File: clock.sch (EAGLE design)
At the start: 15 parts, among them IC1 MEGA16-P

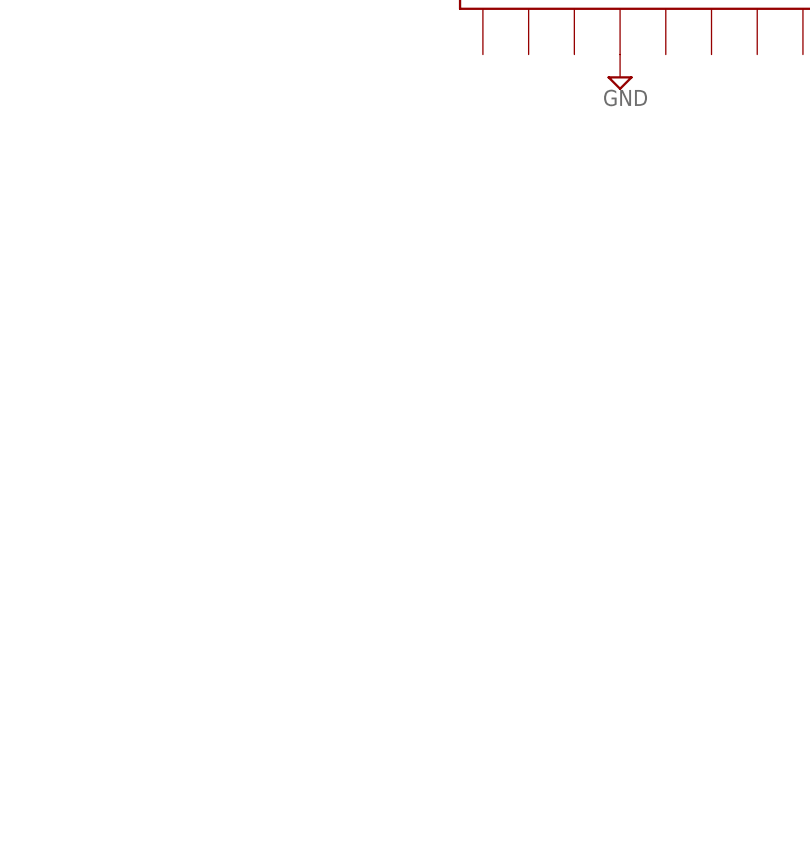
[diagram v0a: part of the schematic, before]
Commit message: 1.1
added smd leds and bugfixed a route.
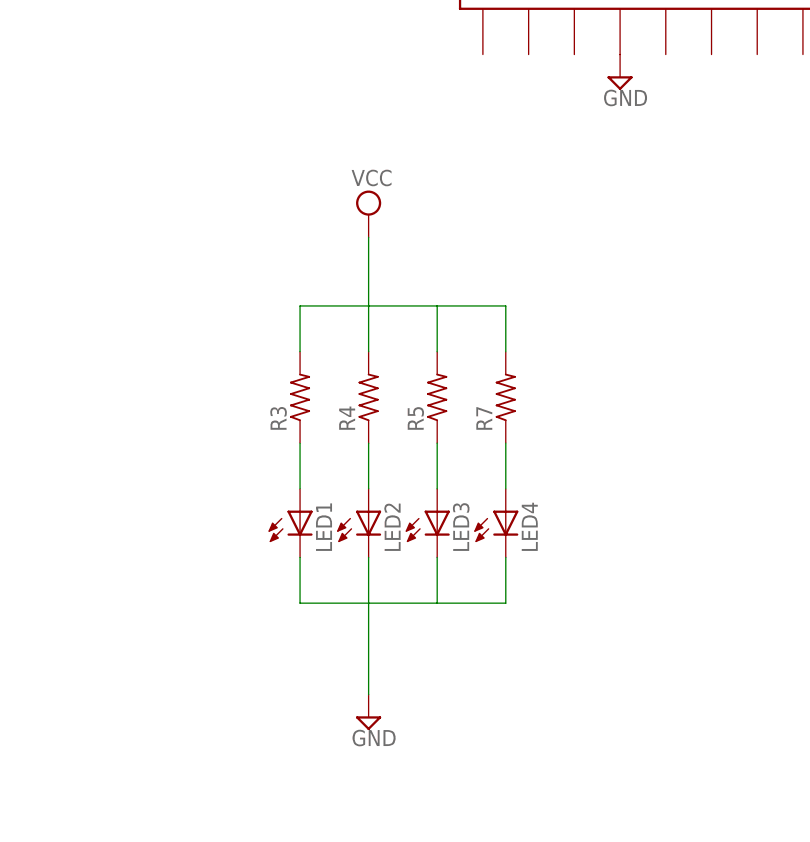
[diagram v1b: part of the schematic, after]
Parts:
- added LED1, LED2, LED3, LED4: (no value), eagle-ltspice:LED_ESML0603
- added R3, R4, R5, R7: (no value), resistor:R-US_R0603
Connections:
- new net N$15: LED1.A, R3.1
- new net N$18: LED2.A, R4.1
- new net N$27: LED3.A, R5.1
- new net N$28: LED4.A, R7.1
- net GND: now also LED1.C, LED2.C, LED3.C, LED4.C
- net VCC: now also R3.2, R4.2, R5.2, R7.2
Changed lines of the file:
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@@
 <layer number="97" name="Info" color="7" fill="1" visible="yes" active="yes"/>
 <layer number="98" name="Guide" color="6" fill="1" visible="yes" active="yes"/>
+<layer number="99" name="SpiceOrder" color="5" fill="1" visible="yes" active="yes"/>
 </layers>
 <schematic xreflabel="%F%N/%S.%C%R" xrefpart="/%S.%C%R">
@@
 <part name="SUPPLY13" library="supply2" deviceset="GND" device=""/>
 <part name="SUPPLY14" library="supply2" deviceset="VCC" device=""/>
+<part name="LED1" library="eagle-ltspice" deviceset="LED_E" device="SML0603"/>
+<part name="LED2" library="eagle-ltspice" deviceset="LED_E" device="SML0603"/>
+<part name="LED3" library="eagle-ltspice" deviceset="LED_E" device="SML0603"/>
+<part name="LED4" library="eagle-ltspice" deviceset="LED_E" device="SML0603"/>
+<part name="R3" library="resistor" deviceset="R-US_" device="R0603"/>
+<part name="R4" library="resistor" deviceset="R-US_" device="R0603"/>
+<part name="R5" library="resistor" deviceset="R-US_" device="R0603"/>
+<part name="R7" library="resistor" deviceset="R-US_" device="R0603"/>
+<part name="SUPPLY15" library="supply2" deviceset="VCC" device=""/>
+<part name="SUPPLY16" library="supply2" deviceset="GND" device=""/>
 </parts>
 <sheets>
@@
 <instance part="SUPPLY13" gate="GND" x="5.08" y="-17.78"/>
 <instance part="SUPPLY14" gate="G$1" x="-12.7" y="68.58" rot="R90"/>
+<instance part="LED1" gate="G$1" x="172.72" y="12.7"/>
+<instance part="LED2" gate="G$1" x="180.34" y="12.7"/>
+<instance part="LED3" gate="G$1" x="187.96" y="12.7"/>
+<instance part="LED4" gate="G$1" x="195.58" y="12.7"/>
+<instance part="R3" gate="G$1" x="172.72" y="25.4" rot="R90"/>
+<instance part="R4" gate="G$1" x="180.34" y="25.4" rot="R90"/>
+<instance part="R5" gate="G$1" x="187.96" y="25.4" rot="R90"/>
+<instance part="R7" gate="G$1" x="195.58" y="25.4" rot="R90"/>
+<instance part="SUPPLY15" gate="G$1" x="180.34" y="45.72"/>
+<instance part="SUPPLY16" gate="GND" x="180.34" y="-10.16"/>
 </instances>
 <busses>
@@
 <junction x="5.08" y="-15.24"/>
 </segment>
+<segment>
+<pinref part="LED1" gate="G$1" pin="C"/>
+<wire x1="172.72" y1="7.62" x2="172.72" y2="2.54" width="0.1524" layer="91"/>
+<pinref part="LED4" gate="G$1" pin="C"/>
+<wire x1="172.72" y1="2.54" x2="180.34" y2="2.54" width="0.1524" layer="91"/>
+<wire x1="180.34" y1="2.54" x2="187.96" y2="2.54" width="0.1524" layer="91"/>
+<wire x1="187.96" y1="2.54" x2="195.58" y2="2.54" width="0.1524" layer="91"/>
+<wire x1="195.58" y1="2.54" x2="195.58" y2="7.62" width="0.1524" layer="91"/>
+<pinref part="LED3" gate="G$1" pin="C"/>
+<wire x1="187.96" y1="7.62" x2="187.96" y2="2.54" width="0.1524" layer="91"/>
+<pinref part="LED2" gate="G$1" pin="C"/>
+<wire x1="180.34" y1="7.62" x2="180.34" y2="2.54" width="0.1524" layer="91"/>
+<pinref part="SUPPLY16" gate="GND" pin="GND"/>
+<wire x1="180.34" y1="-7.62" x2="180.34" y2="2.54" width="0.1524" layer="91"/>
+</segment>
 </net>
 <net name="N$19" class="0">
@@
 <junction x="-10.16" y="68.58"/>
 </segment>
+<segment>
+<pinref part="R3" gate="G$1" pin="2"/>
+<wire x1="172.72" y1="30.48" x2="172.72" y2="35.56" width="0.1524" layer="91"/>
+<pinref part="R7" gate="G$1" pin="2"/>
+<wire x1="172.72" y1="35.56" x2="180.34" y2="35.56" width="0.1524" layer="91"/>
+<wire x1="180.34" y1="35.56" x2="187.96" y2="35.56" width="0.1524" layer="91"/>
+<wire x1="187.96" y1="35.56" x2="195.58" y2="35.56" width="0.1524" layer="91"/>
+<wire x1="195.58" y1="35.56" x2="195.58" y2="30.48" width="0.1524" layer="91"/>
+<pinref part="R5" gate="G$1" pin="2"/>
+<wire x1="187.96" y1="35.56" x2="187.96" y2="30.48" width="0.1524" layer="91"/>
+<pinref part="R4" gate="G$1" pin="2"/>
+<wire x1="180.34" y1="35.56" x2="180.34" y2="30.48" width="0.1524" layer="91"/>
+<pinref part="SUPPLY15" gate="G$1" pin="VCC"/>
+<wire x1="180.34" y1="43.18" x2="180.34" y2="35.56" width="0.1524" layer="91"/>
+</segment>
 </net>
 <net name="N$22" class="0">
@@
 </segment>
 </net>
+<net name="N$15" class="0">
+<segment>
+<pinref part="R3" gate="G$1" pin="1"/>
+<pinref part="LED1" gate="G$1" pin="A"/>
+<wire x1="172.72" y1="20.32" x2="172.72" y2="15.24" width="0.1524" layer="91"/>
+</segment>
+</net>
+<net name="N$18" class="0">
+<segment>
+<pinref part="R4" gate="G$1" pin="1"/>
+<pinref part="LED2" gate="G$1" pin="A"/>
+<wire x1="180.34" y1="20.32" x2="180.34" y2="15.24" width="0.1524" layer="91"/>
+</segment>
+</net>
+<net name="N$27" class="0">
+<segment>
+<pinref part="R5" gate="G$1" pin="1"/>
+<pinref part="LED3" gate="G$1" pin="A"/>
+<wire x1="187.96" y1="20.32" x2="187.96" y2="15.24" width="0.1524" layer="91"/>
+</segment>
+</net>
+<net name="N$28" class="0">
+<segment>
+<pinref part="R7" gate="G$1" pin="1"/>
+<pinref part="LED4" gate="G$1" pin="A"/>
+<wire x1="195.58" y1="20.32" x2="195.58" y2="15.24" width="0.1524" layer="91"/>
+</segment>
+</net>
